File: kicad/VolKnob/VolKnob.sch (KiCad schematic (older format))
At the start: 3 parts, among them P1 CONNECTOR, SW1 Rotary_Encoder

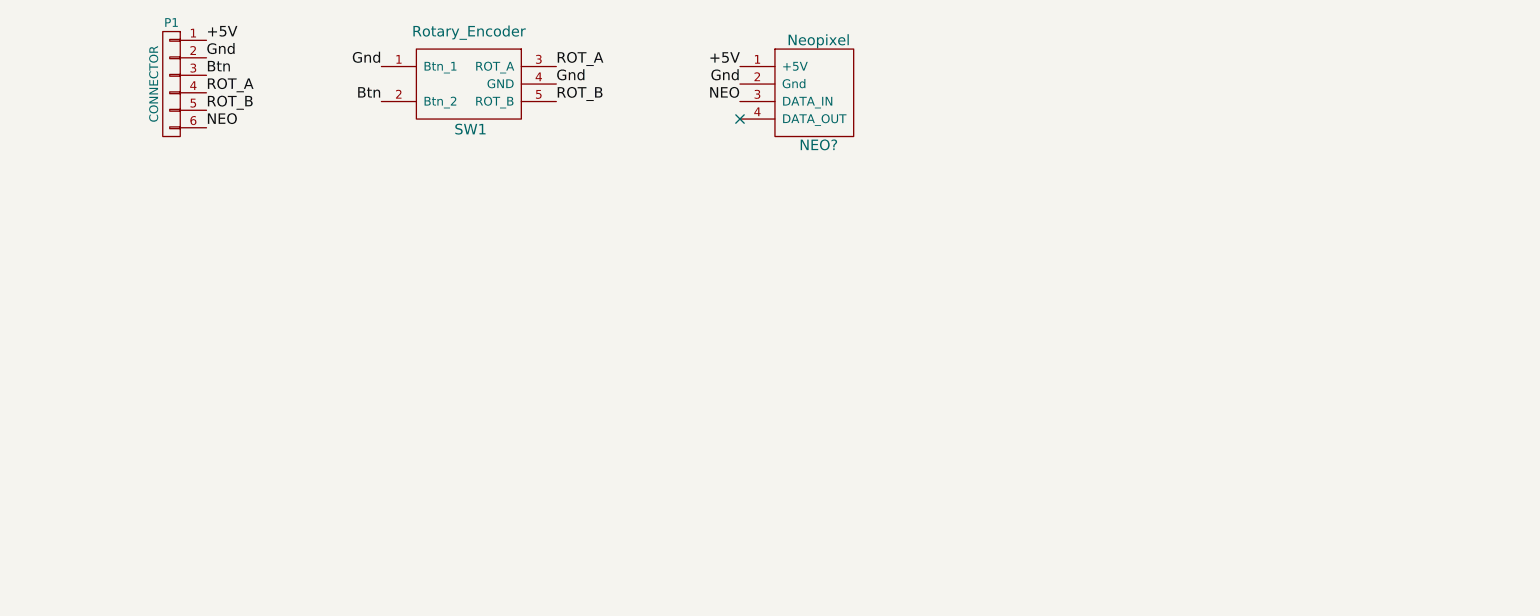
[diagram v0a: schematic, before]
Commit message: Modified circuit to allow for hardware debounce
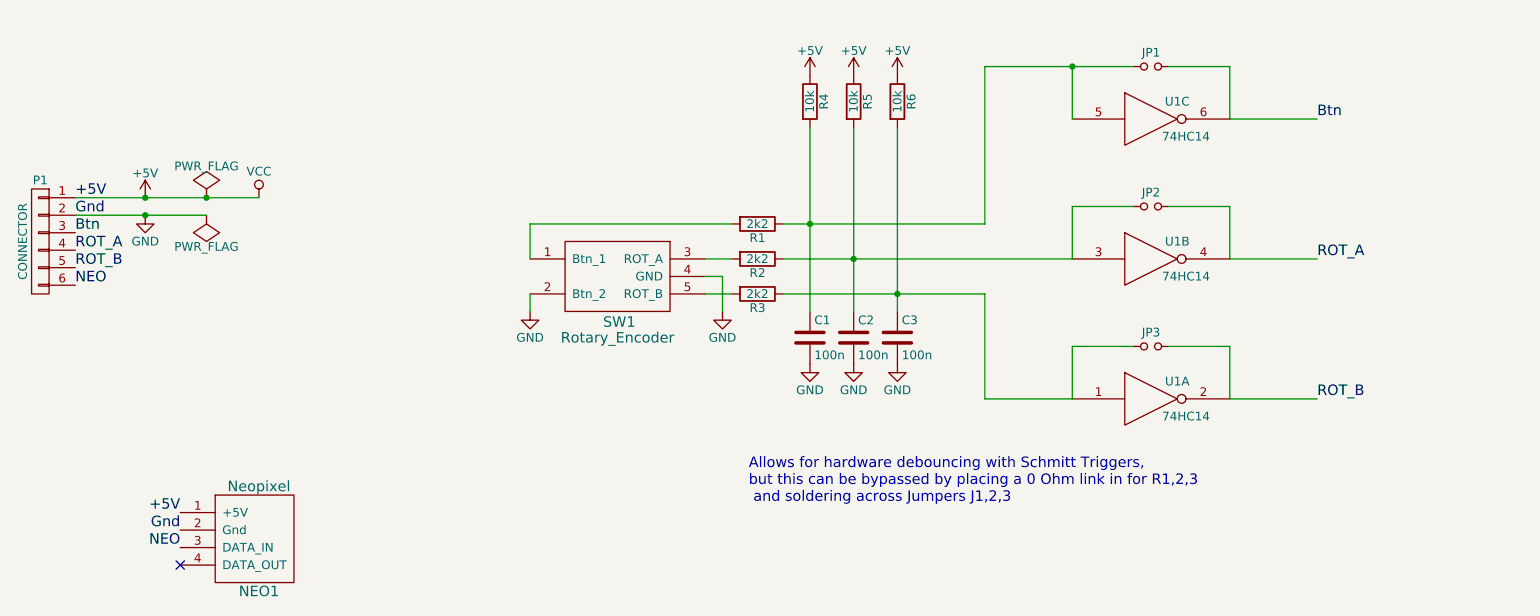
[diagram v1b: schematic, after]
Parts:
- added C1, C2, C3: 100n, Capacitors_SMD:C_0603_HandSoldering, symbol C
- added JP1, JP2, JP3: Jumper_NO_Small, jumpers:Jumper_NO, symbol Jumper_NO_Small
- added R1, R2, R3: 2k2, Resistors_SMD:R_0603_HandSoldering, symbol R
- added R4, R5, R6: 10k, Resistors_SMD:R_0603_HandSoldering, symbol R
- added U1: 74HC14, SMD_Packages:SOIC-14_N, symbol 74HC14
- NEO1: renamed from NEO?; footprint (none) -> NeoPixel:NeoPixel_Ring_12
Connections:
- net +5V: now also R4.1, R5.1, R6.1, U1.14 (VCC), U1.14 (VCC), U1.14 (VCC)
- net Btn: now also JP1.2, U1.6; no longer SW1.2 (Btn_2)
- net ROT_A: now also JP2.2, U1.4; no longer SW1.3 (ROT_A)
- net ROT_B: now also JP3.2, U1.2; no longer SW1.5 (ROT_B)
- net Gnd renamed GND
- net GND: now also SW1.2 (Btn_2), C1.2, C2.2, C3.2, U1.7 (GND), U1.7 (GND), U1.7 (GND); no longer SW1.1 (Btn_1)
- new net: R1.2, SW1.1 (Btn_1)
- new net: R2.2, SW1.3 (ROT_A)
- new net: R3.2, SW1.5 (ROT_B)
- new net: C2.1, JP2.1, R2.1, R5.2, U1.3
- new net: C3.1, JP3.1, R3.1, R6.2, U1.1
- new net: C1.1, JP1.1, R1.1, R4.2, U1.5
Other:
- note added: "Allows for hardware debouncing with Schmitt Triggers, \nbut this can be bypassed by placing a 0 Ohm link in for R1,2,3\n and soldering across Jumpers J1,2,3"
- moved on the sheet: NEO1, P1, SW1

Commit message: Minor updates and board submitted for fabrication
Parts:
- added D1, D2, D3: LED, SMD_LED:LED_SMD_1.6x0.8mm, symbol LED
- added R7, R8, R9: 220, Resistors_SMD:R_0603_HandSoldering, symbol R
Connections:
- net Btn: now also D1.2 (A)
- net GND: now also R7.1, R8.1, R9.1
- net ROT_A: now also D2.2 (A)
- net ROT_B: now also D3.2 (A)
- new net: D1.1 (K), R7.2
- new net: D2.1 (K), R8.2
- new net: D3.1 (K), R9.2
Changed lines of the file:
@@
 Connection ~ 7000 2700
 Wire Wire Line
-	7900 3000 8400 3000
+	7900 3000 8800 3000
 Wire Wire Line
-	7900 3800 8400 3800
+	7900 3800 8800 3800
 Wire Wire Line
-	7900 4600 8400 4600
+	7900 4600 8800 4600
 $Comp
 L PWR_FLAG #FLG011
@@
 Text Notes 5150 5200 0    60   ~ 0
 Allows for hardware debouncing with Schmitt Triggers, \nbut this can be bypassed by placing a 0 Ohm link in for R1,2,3\n and soldering across Jumpers J1,2,3
+$Comp
+L LED D1
+U 1 1 5763D1E7
+P 9000 3000
+F 0 "D1" H 9000 3100 50  0000 C CNN
+F 1 "LED" H 9000 2900 50  0000 C CNN
+F 2 "SMD_LED:LED_SMD_1.6x0.8mm" H 9000 3000 50  0001 C CNN
+F 3 "" H 9000 3000 50  0000 C CNN
+	1    9000 3000
+	-1   0    0    1
+$EndComp
+$Comp
+L R R7
+U 1 1 5763D252
+P 9350 3000
+F 0 "R7" V 9430 3000 50  0000 C CNN
+F 1 "220" V 9350 3000 50  0000 C CNN
+F 2 "Resistors_SMD:R_0603_HandSoldering" V 9280 3000 50  0001 C CNN
+F 3 "" H 9350 3000 50  0000 C CNN
+	1    9350 3000
+	0    1    1    0
+$EndComp
+$Comp
+L GND #PWR014
+U 1 1 5763D29B
+P 9500 3000
+F 0 "#PWR014" H 9500 2750 50  0001 C CNN
+F 1 "GND" H 9500 2850 50  0000 C CNN
+F 2 "" H 9500 3000 50  0000 C CNN
+F 3 "" H 9500 3000 50  0000 C CNN
+	1    9500 3000
+	1    0    0    -1
+$EndComp
+$Comp
+L LED D2
+U 1 1 5763D31D
+P 9000 3800
+F 0 "D2" H 9000 3900 50  0000 C CNN
+F 1 "LED" H 9000 3700 50  0000 C CNN
+F 2 "SMD_LED:LED_SMD_1.6x0.8mm" H 9000 3800 50  0001 C CNN
+F 3 "" H 9000 3800 50  0000 C CNN
+	1    9000 3800
+	-1   0    0    1
+$EndComp
+$Comp
+L R R8
+U 1 1 5763D323
+P 9350 3800
+F 0 "R8" V 9430 3800 50  0000 C CNN
+F 1 "220" V 9350 3800 50  0000 C CNN
+F 2 "Resistors_SMD:R_0603_HandSoldering" V 9280 3800 50  0001 C CNN
+F 3 "" H 9350 3800 50  0000 C CNN
+	1    9350 3800
+	0    1    1    0
+$EndComp
+$Comp
+L GND #PWR015
+U 1 1 5763D329
+P 9500 3800
+F 0 "#PWR015" H 9500 3550 50  0001 C CNN
+F 1 "GND" H 9500 3650 50  0000 C CNN
+F 2 "" H 9500 3800 50  0000 C CNN
+F 3 "" H 9500 3800 50  0000 C CNN
+	1    9500 3800
+	1    0    0    -1
+$EndComp
+$Comp
+L LED D3
+U 1 1 5763D38B
+P 9000 4600
+F 0 "D3" H 9000 4700 50  0000 C CNN
+F 1 "LED" H 9000 4500 50  0000 C CNN
+F 2 "SMD_LED:LED_SMD_1.6x0.8mm" H 9000 4600 50  0001 C CNN
+F 3 "" H 9000 4600 50  0000 C CNN
+	1    9000 4600
+	-1   0    0    1
+$EndComp
+$Comp
+L R R9
+U 1 1 5763D391
+P 9350 4600
+F 0 "R9" V 9430 4600 50  0000 C CNN
+F 1 "220" V 9350 4600 50  0000 C CNN
+F 2 "Resistors_SMD:R_0603_HandSoldering" V 9280 4600 50  0001 C CNN
+F 3 "" H 9350 4600 50  0000 C CNN
+	1    9350 4600
+	0    1    1    0
+$EndComp
+$Comp
+L GND #PWR016
+U 1 1 5763D397
+P 9500 4600
+F 0 "#PWR016" H 9500 4350 50  0001 C CNN
+F 1 "GND" H 9500 4450 50  0000 C CNN
+F 2 "" H 9500 4600 50  0000 C CNN
+F 3 "" H 9500 4600 50  0000 C CNN
+	1    9500 4600
+	1    0    0    -1
+$EndComp
 $EndSCHEMATC
